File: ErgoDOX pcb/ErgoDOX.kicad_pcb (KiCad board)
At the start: 2 copper layers, 182.8 x 158.9 mm, 96 parts, among them J10 USB VCC, J2 3.5mm, J3 JMP, J4 JMP, J6 USB_C_Receptacle_USB2.0, J7 PROG, J8 JTAG, J9 USB GND, SW0:10 SW0:3, SW0:11 SW0:2, SW0:12 SW0:1, SW0:7 SW0:6, SW0:8 SW0:5, SW0:9 SW0:4, SW1:10 SW1:3, SW1:11 SW1:2, SW1:12 SW1:1, SW1:13 SW1:0, SW1:9 SW1:4, SW2:10 SW2:3, SW2:11 SW2:2, SW2:12 SW2:1, SW2:13 SW2:0, SW2:7 SW2:6, SW2:8 SW2:5, SW2:9 SW2:4, SW3:10 SW3:3, SW3:11 SW3:2, SW3:12 SW3:1, SW3:13 SW3:0, SW3:8 SW3:5, SW3:9 SW3:4, SW4:10 SW4:3, SW4:11 SW4:2, SW4:12 SW4:1, SW4:13 SW4:0, SW4:7 SW4:6, SW4:8 SW4:5, SW4:9 SW4:4, SW5:10 SW5:3, SW5:11 SW5:2, SW5:12 SW5:1, SW5:13 SW5:0, SW5:7 SW5:6, SW5:8 SW5:5, SW5:9 SW5:4, U1 LM337_SOT223, U2 ESP32-S3 LH, U3 ESP32-S3 RH

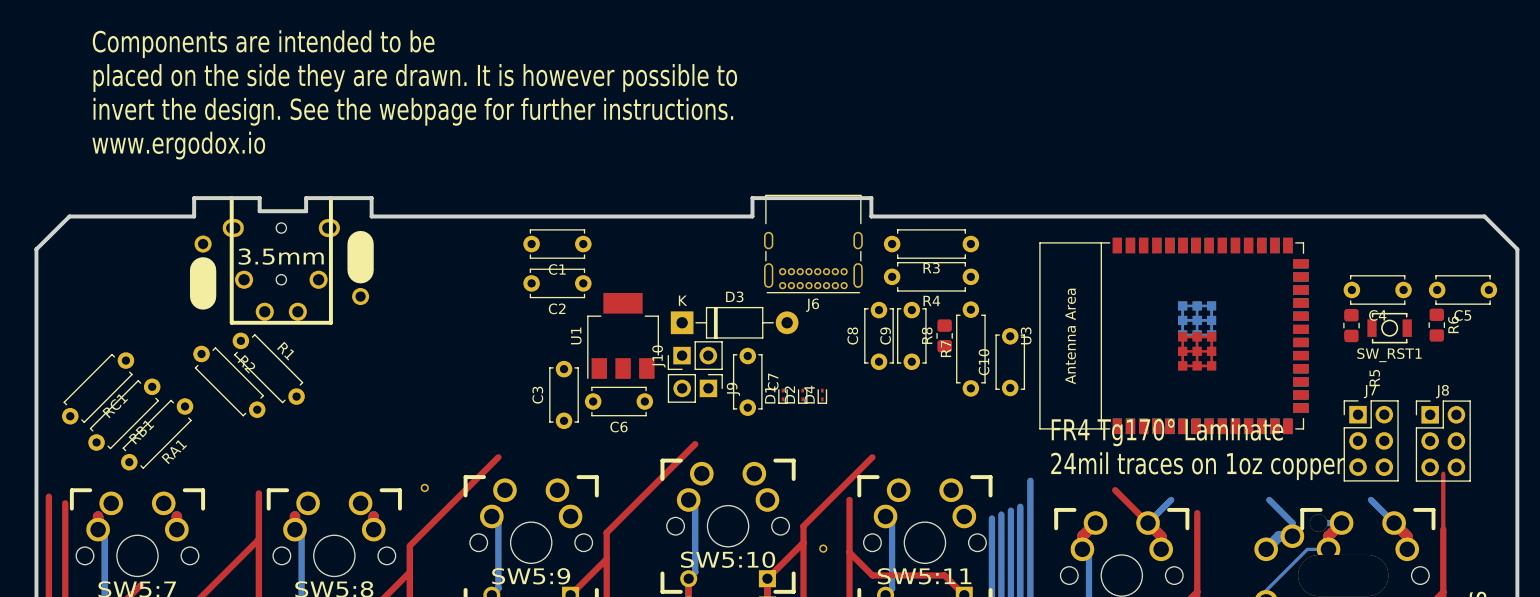
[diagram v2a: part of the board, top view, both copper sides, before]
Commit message: Place components in more final layout
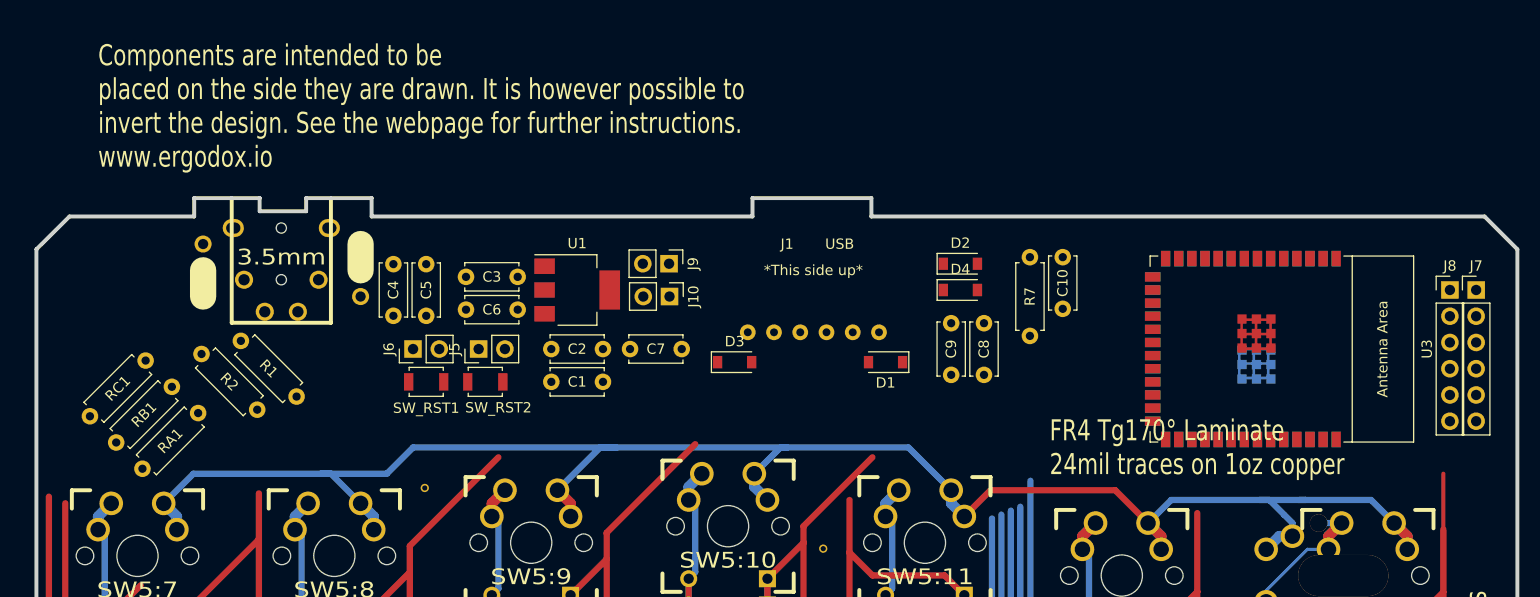
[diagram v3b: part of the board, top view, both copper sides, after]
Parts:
- removed R3, R4: 5.1k, Resistor_THT:R_Axial_DIN0207_L6.3mm_D2.5mm_P7.62mm_Horizontal
- removed R5, R6, R8: 0, Resistor_SMD:R_0805_2012Metric_Pad1.20x1.40mm_HandSolder
- added J1: USB, ErgoDOX pcb:SF USB-C Breakout, F.Cu at (137.8, 37.5)
- added J5: BT_JMP, Connector_PinHeader_2.54mm:PinHeader_1x02_P2.54mm_Vertical, F.Cu at (105.4, 45.1)
- added SW_RST2: BOOT, Button_Switch_SMD:SW_SPST_B3U-1000P, F.Cu at (106.0, 48.3)
- D1, D2, D4: value ESD9B3.3ST5G -> SMF9.0CA; footprint Diode_SMD:D_SOD-923 -> Diode_SMD:D_SOD-123
- D3: value 1N5819 -> 1N5819HW-7-F; footprint Diode_THT:D_DO-41_SOD81_P10.16mm_Horizontal -> Diode_SMD:D_SOD-123
- J6: value USB_C_Receptacle_USB2.0 -> EN_JMP; footprint Connector_USB:USB_C_Receptacle_GCT_USB4085 -> Connector_PinHeader_2.54mm:PinHeader_1x02_P2.54mm_Vertical
- J7, J8: footprint Connector_PinHeader_2.54mm:PinHeader_2x03_P2.54mm_Vertical -> Connector_PinHeader_2.54mm:PinHeader_1x06_P2.54mm_Vertical
- SW_RST1: value SWITCH_PUSH -> RST; footprint Buttons_Switches_SMD:SW_SPST_B3U-1000P -> Button_Switch_SMD:SW_SPST_B3U-1000P
- moved C5 102.9 mm to (100.3, 36.9), turned to -90 degrees
- moved C4 97.8 mm to (97.2, 36.9), turned to -90 degrees
- moved SW_RST1 93.4 mm to (100.3, 48.3), turned to 0 degrees
- moved J6 42.2 mm to (99.1, 45.1), turned to 90 degrees
- moved D2 19.9 mm to (152.0, 36.8), turned to 0 degrees
- moved D4 16.8 mm to (152.0, 39.4), turned to 0 degrees
- moved J7 16.6 mm to (201.9, 39.4)
- moved C6 15.2 mm to (109.2, 41.3)
- moved C3 14.6 mm to (109.2, 38.1), turned to 180 degrees
- moved R7 13.9 mm to (158.8, 36.2), turned to -90 degrees
- moved C1 13.7 mm to (112.4, 48.3), turned to 0 degrees
- moved C10 13.6 mm to (161.9, 36.2), turned to -90 degrees
- moved J9 12.7 mm to (123.8, 36.8)
- moved J8 12.2 mm to (199.4, 39.4)
- moved C8 10.8 mm to (154.3, 42.6), turned to -90 degrees
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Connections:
- D1:7 pad 2: /COL6 -> COL6
- D1:8 pad 2: /COL5 -> COL5
- J7 pad 1: /EN -> VCC
- J7 pad 2: VCC -> GND
- J7 pad 4: GND -> U0RXD
- J7 pad 5: U0RXD -> /EN
- J9 pad 1: Net-(J6-PadA1) -> Net-(J9-Pad1)
- R7 pad 2: /ESP_3V3 -> VCC
- STAR_1 pad 0: (no net) -> COL4
- STAR_1 pad 1: (no net) -> COL3
- STAR_1 pad 2: (no net) -> COL3
- STAR_1 pad 3: (no net) -> COL4
- STAR_1 pad 4: (no net) -> COL4
- STAR_2 pad 5: (no net) -> ROW1
- STAR_2 pad 6: (no net) -> ROW1
- SW0:10 pad 1: /ROW0 -> ROW0
- SW0:10 pad 4: /COL10 -> COL3
- SW0:11 pad 1: /ROW0 -> ROW0
- SW0:11 pad 4: /COL11 -> COL11
- SW0:12 pad 1: /ROW0 -> ROW0
- SW0:12 pad 4: /COL1 -> COL1
- SW0:7 pad 1: /ROW0 -> ROW0
- SW0:7 pad 4: /COL6 -> COL6
- SW0:8 pad 1: /ROW0 -> ROW0
- SW0:8 pad 4: /COL5 -> COL5
- SW0:9 pad 1: /ROW0 -> ROW0
- SW0:9 pad 4: /COL4 -> COL4
- SW1:10 pad 1: /ROW1 -> ROW1
- SW1:10 pad 4: /COL10 -> COL3
- SW1:11 pad 1: /ROW1 -> ROW1
- SW1:11 pad 4: /COL11 -> COL11
- SW1:12 pad 1: /ROW1 -> ROW1
- SW1:12 pad 4: /COL1 -> COL1
- SW1:13 pad 1: /ROW1 -> ROW1
- SW1:13 pad 4: /COL0 -> COL0
- SW1:9 pad 1: /ROW1 -> ROW1
- SW1:9 pad 4: /COL4 -> COL4
- SW2:10 pad 1: /ROW2 -> ROW2
- SW2:10 pad 4: /COL10 -> COL3
- SW2:11 pad 1: /ROW2 -> ROW2
- SW2:11 pad 4: /COL11 -> COL11
- SW2:12 pad 1: /ROW2 -> ROW2
- SW2:12 pad 4: /COL1 -> COL1
- SW2:13 pad 1: /ROW2 -> ROW2
- SW2:13 pad 4: /COL0 -> COL0
- SW2:7 pad 1: /ROW2 -> ROW2
- SW2:7 pad 4: /COL6 -> COL6
- SW2:8 pad 1: /ROW2 -> ROW2
- SW2:8 pad 4: /COL5 -> COL5
- SW2:9 pad 1: /ROW2 -> ROW2
- SW2:9 pad 4: /COL4 -> COL4
- SW3:10 pad 1: /ROW3 -> ROW3
- SW3:10 pad 4: /COL10 -> COL3
- SW3:11 pad 1: /ROW3 -> ROW3
- SW3:11 pad 4: /COL11 -> COL11
- SW3:12 pad 1: /ROW3 -> ROW3
- SW3:12 pad 4: /COL1 -> COL1
- SW3:13 pad 1: /ROW3 -> ROW3
- SW3:13 pad 4: /COL0 -> COL0
- SW3:8 pad 1: /ROW3 -> ROW3
- SW3:8 pad 4: /COL5 -> COL5
- SW3:9 pad 1: /ROW3 -> ROW3
- SW3:9 pad 4: /COL4 -> COL4
- SW4:10 pad 1: /ROW4 -> ROW4
- SW4:10 pad 4: /COL10 -> COL3
- SW4:11 pad 1: /ROW4 -> ROW4
- SW4:11 pad 4: /COL11 -> COL11
- SW4:12 pad 1: /ROW4 -> ROW4
- SW4:12 pad 4: /COL1 -> COL1
- SW4:13 pad 1: /ROW4 -> ROW4
- SW4:13 pad 4: /COL0 -> COL0
- SW4:7 pad 1: /ROW4 -> ROW4
- SW4:7 pad 4: /COL6 -> COL6
- SW4:8 pad 1: /ROW4 -> ROW4
- SW4:8 pad 4: /COL5 -> COL5
- SW4:9 pad 1: /ROW4 -> ROW4
- SW4:9 pad 4: /COL4 -> COL4
- SW5:10 pad 1: /ROW5 -> ROW5
- SW5:10 pad 4: /COL10 -> COL3
- SW5:11 pad 1: /ROW5 -> ROW5
- SW5:11 pad 4: /COL11 -> COL11
- SW5:12 pad 1: /ROW5 -> ROW5
- SW5:12 pad 4: /COL1 -> COL1
- SW5:13 pad 1: /ROW5 -> ROW5
- SW5:13 pad 4: /COL0 -> COL0
- SW5:7 pad 1: /ROW5 -> ROW5
- SW5:7 pad 4: /COL6 -> COL6
- SW5:8 pad 1: /ROW5 -> ROW5
- SW5:8 pad 4: /COL5 -> COL5
- SW5:9 pad 1: /ROW5 -> ROW5
- SW5:9 pad 4: /COL4 -> COL4
- SW_RST1 pad 1: /RST -> Net-(C4-Pad2)
- SX0:10 pad 1: /ROW0 -> ROW0
- SX0:11 pad 1: /ROW0 -> ROW0
- SX1:7 pad 1: /ROW1 -> ROW1
- SX1:8 pad 1: /ROW1 -> ROW1
- U2 pad 2: /ESP_3V3 -> VCC
- U2 pad 23: COL10 -> COL3
- U3 pad 2: /ESP_3V3 -> VCC
- U3 pad 23: COL10 -> COL3
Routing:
- net ROW0: track 0.00 -> 363.5 mm
- net /ROW0: track 363.5 -> 0.00 mm
- net ROW1: track 0.00 -> 276.5 mm
- net /ROW1: track 276.5 -> 0.00 mm
- net COL1: track 0.00 -> 268.8 mm
- net /COL1: track 268.8 -> 0.00 mm
- net COL11: track 0.00 -> 262.9 mm
- net /COL11: track 262.9 -> 0.00 mm
- net ROW2: track 0.00 -> 254.3 mm
- net /ROW2: track 254.3 -> 0.00 mm
- net COL4: track 0.00 -> 222.7 mm
- net /COL4: track 222.7 -> 0.00 mm
- net ROW4: track 0.00 -> 217.9 mm
- net /ROW4: track 217.9 -> 0.00 mm
- net ROW3: track 0.00 -> 198.5 mm
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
